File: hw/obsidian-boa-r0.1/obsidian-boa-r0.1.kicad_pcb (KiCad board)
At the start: 4 copper layers, 35.6 x 17.8 mm, 90 parts, among them J1 USB_C, J2 PROG, P0 0, P1 1, P10 10, P11 11, P12 12, P13 13, P14 14, P15 15, P16 16, P17 17, P18 18, P19 19, P2 2, P20 20, P21 21, P22 22, P23 23, P24 GND, P25 GND, P26 GND, P27 3V3, P28 3V3, P29 VIN, P3 3, P30 CDONE, P31 CRESET, P32 UP, P33 UP, P34 UP, P35 UP, P4 4, P5 5, P6 6, P7 7, P8 8, P9 9, SW1 TACT, U1 USBLC6-2, U2 W25Q32JVSS, U3 ESP32-S2, U4 W25Q32JVSS, U5 TPS62290, Y1 40MHz

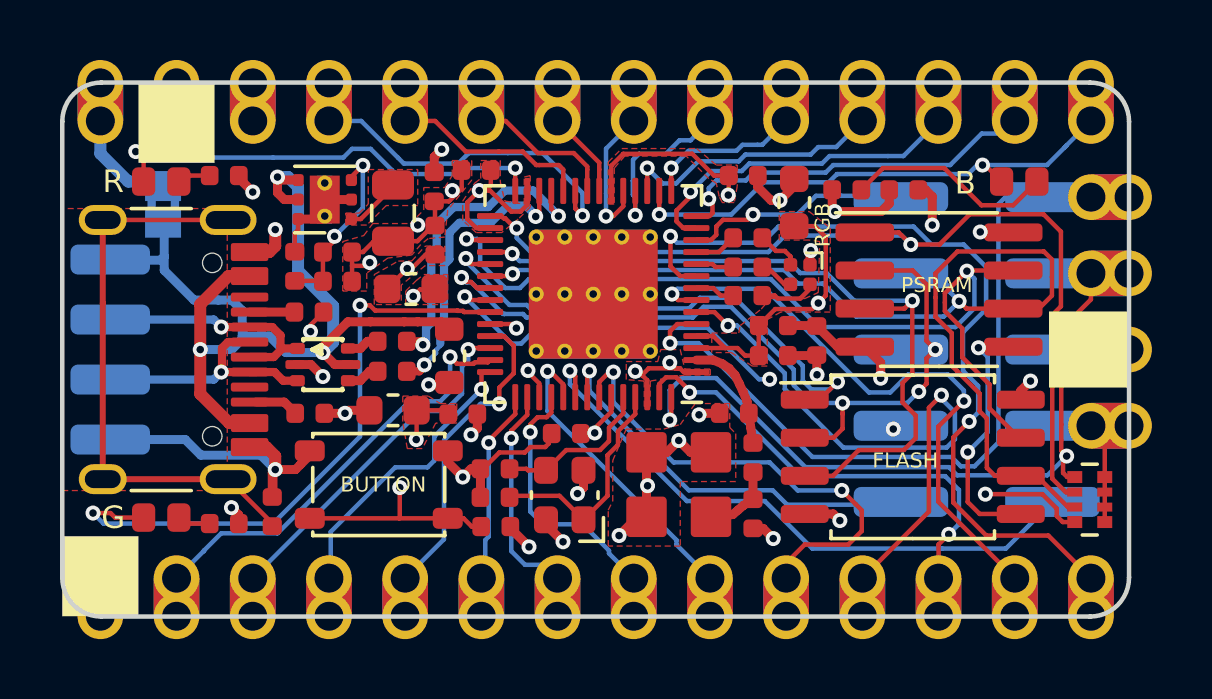
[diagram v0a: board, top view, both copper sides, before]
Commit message: hw.r0d1: update to route VDD_SPI seperately.
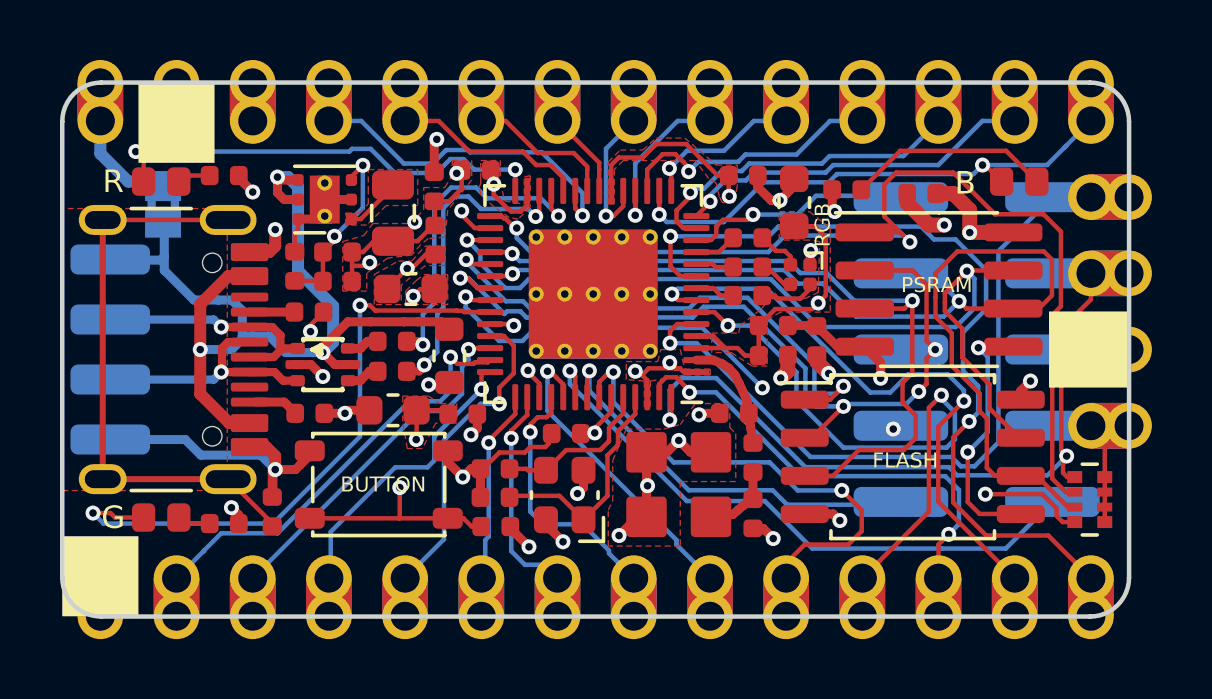
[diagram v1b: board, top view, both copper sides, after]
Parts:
- C1, C2: value 100n -> 2.2uF
- moved C2 0.61 mm to (128.7, 94.8), turned to 180 degrees
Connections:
- C1 pad 1: +3V3 -> /VCC_SPI
- C2 pad 1: +3V3 -> /VCC_SPI
- U2 pad 8: +3V3 -> /VCC_SPI
- U3 pad 30: Net-(C19-Pad1) -> /VCC_SPI
- U4 pad 8: +3V3 -> /VCC_SPI
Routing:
- net /VCC_SPI: track 0.00 -> 43.3 mm, vias 0 -> 4
- net +3V3: track 23.5 -> 18.5 mm, vias 12 -> 10
- net /RAM_~CS: track 31.9 -> 35.3 mm
- net Net-(C19-Pad1): track 33.0 -> 31.0 mm
- net /GPIO34-~BTN: track 15.1 -> 16.8 mm
- net /GPIO0-BOOT: track 24.2 -> 23.3 mm
- net /USB_P: track 9.79 -> 10.6 mm
- net GND: track 48.1 -> 48.7 mm
- net /USB_N: track 10.7 -> 11.2 mm
- net /GPIO9: track 12.6 -> 12.1 mm

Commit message: hw: Sync PCB to schematic
Fixes #7
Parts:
- C5: value 10uF -> 10u
- R7: value 180k -> 453k
- R8: value 180k -> 100k
- U2: value W25Q32JVSS -> LY68L6400SLIT
- U4: value W25Q32JVSS -> W25Q128JV
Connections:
- J1 pad A8: /SBU1 -> (no net)
- J1 pad B8: /SBU2 -> (no net)
